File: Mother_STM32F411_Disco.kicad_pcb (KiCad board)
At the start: 2 copper layers, 2 parts

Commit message: boceteando todavia
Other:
- board text added: "Amplificador"
- board text added: "Multiplexor de Audio"
- board text added: "STMF411-Disco"
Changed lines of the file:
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@@
 		)
+	)
+	(gr_rect
+		(start 167 60)
+		(end 215.5 117.5)
+		(stroke
+			(width 0.1)
+			(type default)
+		)
+		(fill no)
+		(layer "F.SilkS")
+	)
+	(gr_rect
+		(start 218 12.75)
+		(end 236 34.25)
+		(stroke
+			(width 0.1)
+			(type default)
+		)
+		(fill no)
+		(layer "F.SilkS")
+	)
+	(gr_rect
+		(start 241 12.75)
+		(end 259 34.25)
+		(stroke
+			(width 0.1)
+			(type default)
+		)
+		(fill no)
+		(layer "F.SilkS")
+	)
+	(gr_rect
+		(start 70.5 24.5)
+		(end 136.5 121.5)
+		(stroke
+			(width 0.1)
+			(type default)
+		)
+		(fill no)
+		(layer "F.SilkS")
+	)
+	(gr_rect
+		(start 194.5 12)
+		(end 212.5 33.5)
+		(stroke
+			(width 0.1)
+			(type default)
+		)
+		(fill no)
+		(layer "F.SilkS")
+	)
+	(gr_text "STMF411-Disco"
+		(at 70.5 121.5 0)
+		(layer "F.SilkS")
+		(effects
+			(font
+				(size 1 1)
+				(thickness 0.1)
+			)
+			(justify left bottom)
+		)
+	)
+	(gr_text "Amplificador"
+		(at 241 34.25 0)
+		(layer "F.SilkS")
+		(effects
+			(font
+				(size 1 1)
+				(thickness 0.1)
+			)
+			(justify left bottom)
+		)
+	)
+	(gr_text "Amplificador"
+		(at 218 34.25 0)
+		(layer "F.SilkS")
+		(effects
+			(font
+				(size 1 1)
+				(thickness 0.1)
+			)
+			(justify left bottom)
+		)
+	)
+	(gr_text "Multiplexor de Audio\n"
+		(at 167 117.5 0)
+		(layer "F.SilkS")
+		(effects
+			(font
+				(size 1 1)
+				(thickness 0.1)
+			)
+			(justify left bottom)
+		)
+	)
+	(gr_text "Amplificador"
+		(at 194.5 33.5 0)
+		(layer "F.SilkS")
+		(effects
+			(font
+				(size 1 1)
+				(thickness 0.1)
+			)
+			(justify left bottom)
+		)
+	)
+	(group ""
+		(members "2fab3fd3-f4d7-4e7b-8b6d-a96610c467cb" "70729842-181e-4080-b271-1663ce8dfaa7")
+	)
+	(group ""
+		(members "d1a54d29-0ff7-45f9-b5e4-6cd1c676e5bf" "e2b95cdf-10a1-4dc4-b970-0cec3a94f96c")
+	)
+	(group ""
+		(members "337aa6e4-fe99-454c-97c6-cfffce0f4d21" "9b0519a3-c9aa-4c5b-8153-00ee1a23a938")
+	)
+	(group ""
+		(members "250b4368-eeb3-4cfe-a6db-56e90e8a5282" "cacae592-f755-4f9d-b2b2-fca2e8c15bf0")
+	)
+	(group ""
+		(members "0da0d133-9946-46c4-b739-db323635e704" "c476d3e7-f70c-42a9-a5f4-4ef6aaca65fd")
 	)
 	(embedded_fonts no)

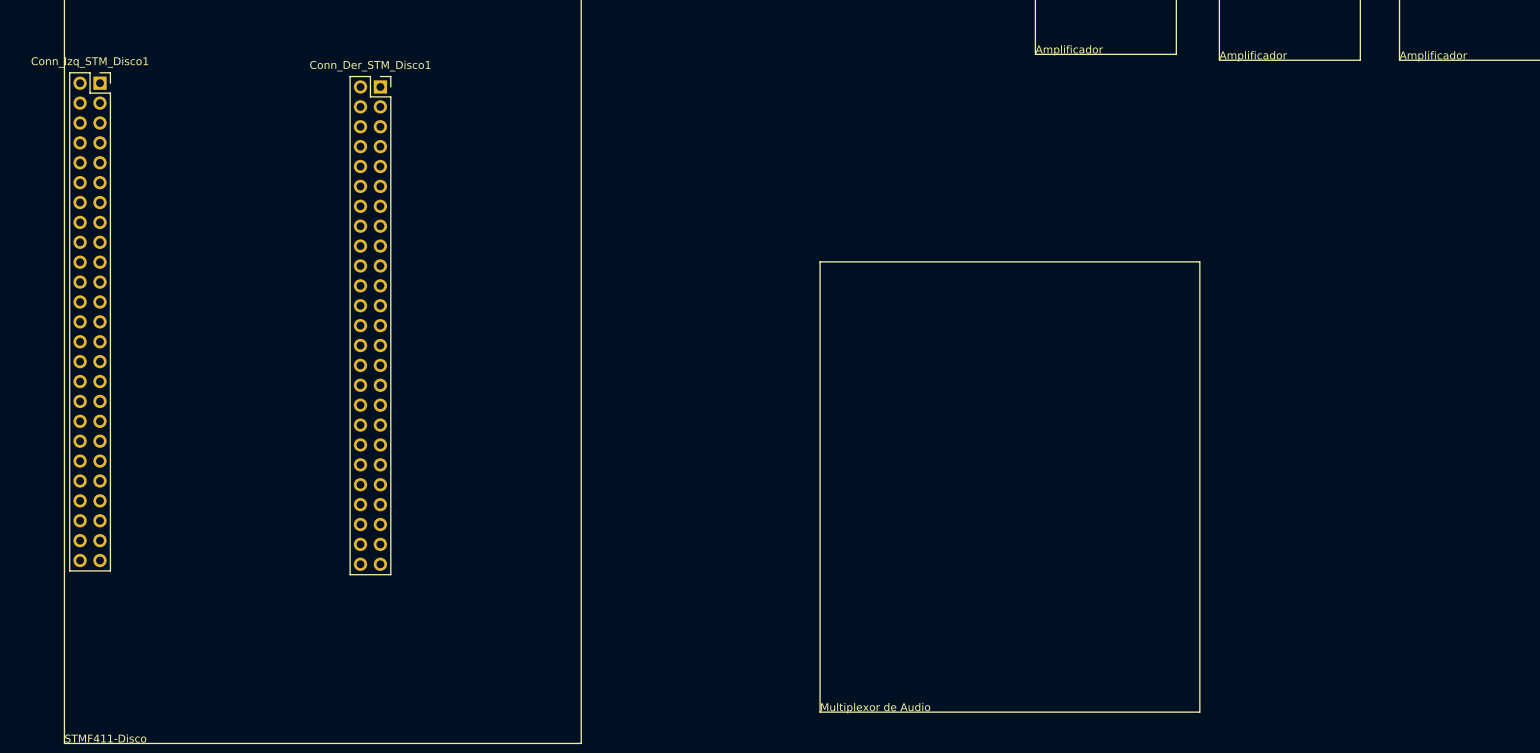
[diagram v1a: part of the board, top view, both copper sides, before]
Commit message: SA-18: placa de esp32 devkitv1 agregada a el esquematico
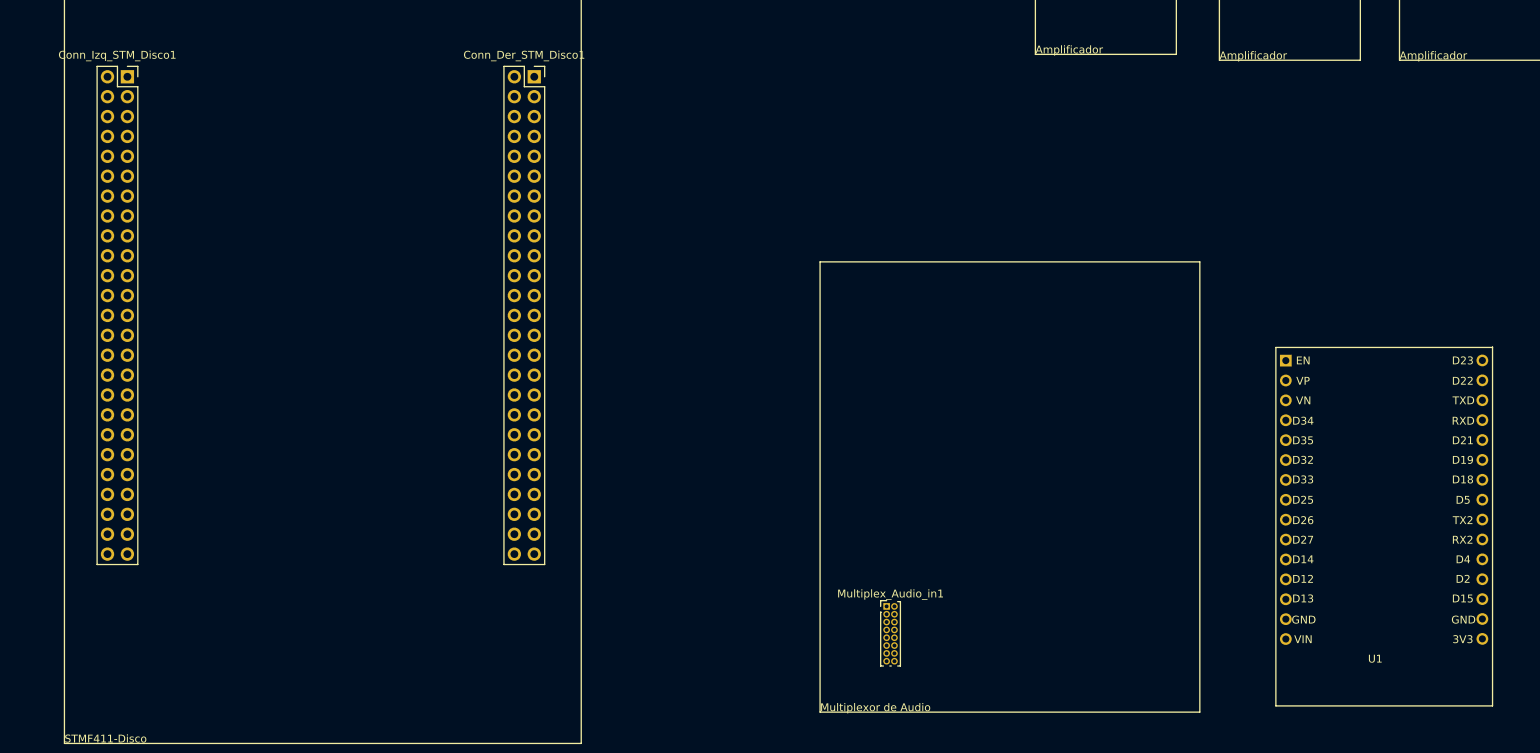
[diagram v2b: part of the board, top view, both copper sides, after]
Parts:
- added Multiplex_Audio_in1: Conn_02x08_Counter_Clockwise, Connector_PinHeader_1.00mm:PinHeader_2x08_P1.00mm_Vertical, F.Cu at (175.5, 104.0)
- added U1: ESP32-DEVKIT-V1, Library:ESP32-C3-DevKitV1, F.Cu at (226.5, 72.6)
- moved Conn_Der_STM_Disco1 19.7 mm to (130.5, 36.4)
- moved Conn_Izq_STM_Disco1 3.59 mm to (78.5, 36.4)

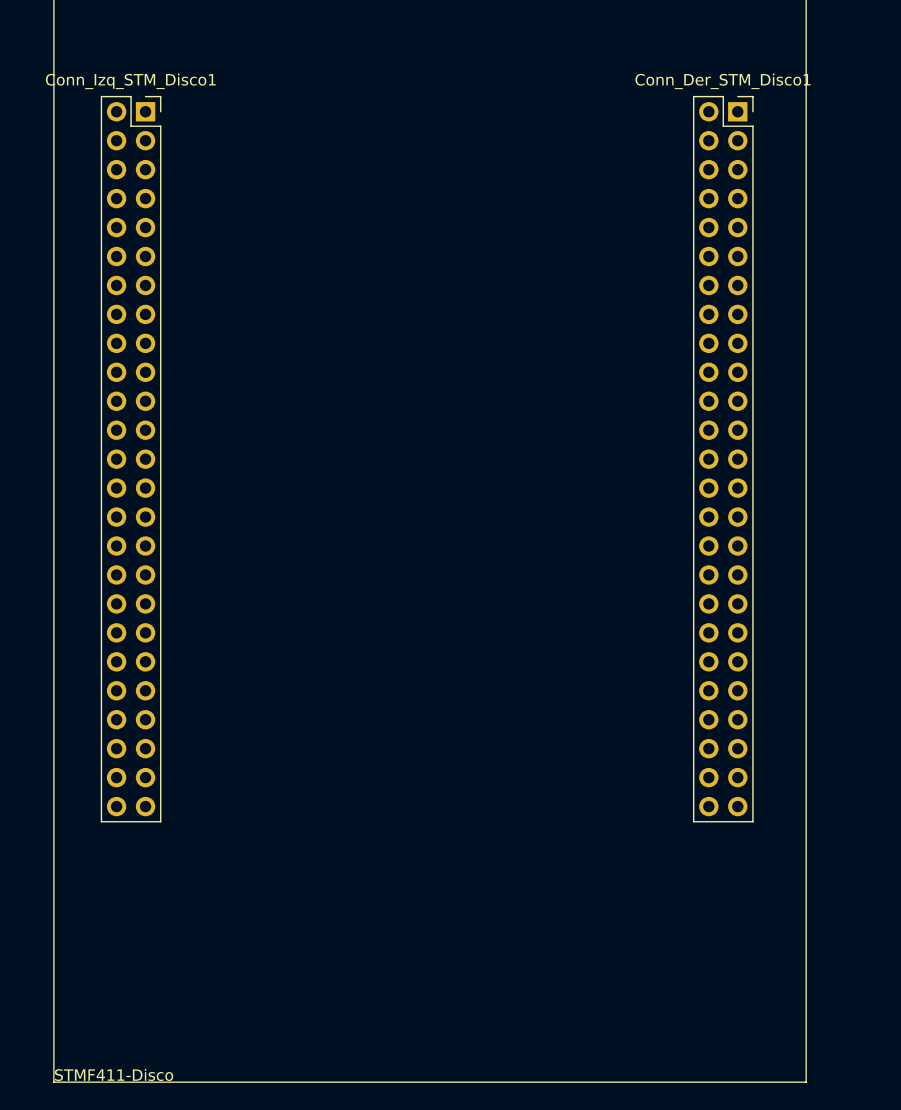
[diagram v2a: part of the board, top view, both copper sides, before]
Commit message: Mudamos librerias a local de proyecto y asignamos 3d models nuevamente
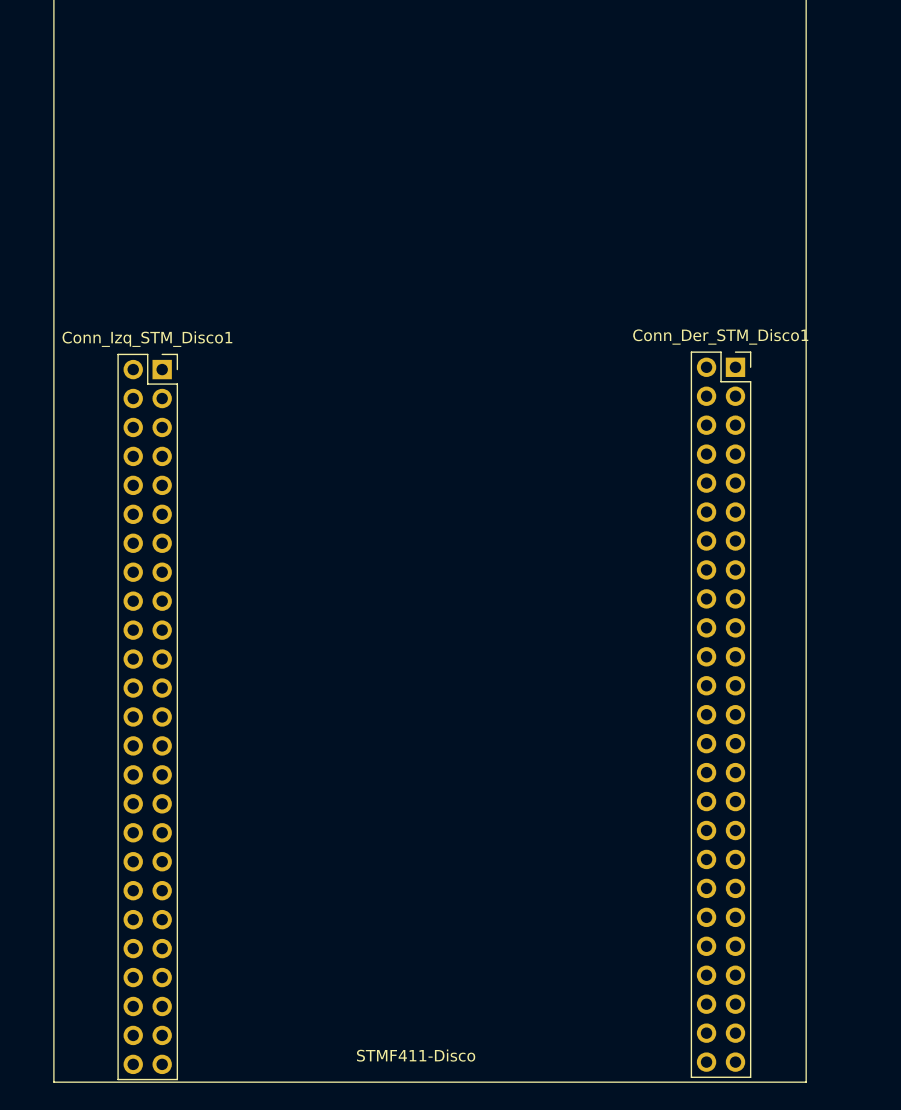
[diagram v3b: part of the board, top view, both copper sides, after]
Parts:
- moved Conn_Izq_STM_Disco1 22.7 mm to (80.0, 59.0)
- moved Conn_Der_STM_Disco1 22.4 mm to (130.3, 58.8)
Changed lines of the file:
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@@
 	(footprint "Connector_PinSocket_2.54mm:PinSocket_2x25_P2.54mm_Vertical"
 		(layer "F.Cu")
-		(at 78.54 36.36)
+		(at 80 58.98)
 		(descr "Through hole straight socket strip, 2x25, 2.54mm pitch, double cols (from Kicad 4.0.7), script generated")
 		(tags "Through hole socket strip THT 2x25 2.54mm double row")
@@
 			)
 		)
+		(model "${KIPRJMOD}/kicad-libraries/3dmodels/stm.3dshapes/STM32F4DISCOVERY--3DModel-STEP-56544.STEP"
+			(offset
+				(xyz 24 -15 8.5)
+			)
+			(scale
+				(xyz 1 1 1)
+			)
+			(rotate
+				(xyz -90 -0 -0)
+			)
+		)
 	)
 	(footprint "Connector_PinSocket_2.54mm:PinSocket_2x25_P2.54mm_Vertical"
 		(layer "F.Cu")
-		(at 130.5 36.36)
+		(at 130.3 58.78)
 		(descr "Through hole straight socket strip, 2x25, 2.54mm pitch, double cols (from Kicad 4.0.7), script generated")
 		(tags "Through hole socket strip THT 2x25 2.54mm double row")
@@
 		)
 		(embedded_fonts no)
-		(model "${KICAD9_3DMODEL_DIR}/RF_Module.3dshapes/ESP32-C3-DevKitM-1.step"
+		(model "${KIPRJMOD}/kicad-libraries/3dmodels/espressif.3dshapes/ESP32-DEVKITC-32D--3DModel-STEP-269445.STEP"
 			(offset
-				(xyz 0 0 0)
+				(xyz 13 -19.5 6)
 			)
 			(scale
@@
 			)
 			(rotate
-				(xyz 0 0 0)
+				(xyz -90 -0 -0)
 			)
 		)
@@
 	)
 	(gr_text "STMF411-Disco"
-		(at 70.5 121.5 0)
+		(at 97 119.8 0)
 		(layer "F.SilkS")
 		(effects
@@
 	)
 	(group ""
-		(members "250b4368-eeb3-4cfe-a6db-56e90e8a5282" "cacae592-f755-4f9d-b2b2-fca2e8c15bf0")
+		(members "0da0d133-9946-46c4-b739-db323635e704" "c476d3e7-f70c-42a9-a5f4-4ef6aaca65fd")
 	)
 	(group ""
-		(members "0da0d133-9946-46c4-b739-db323635e704" "c476d3e7-f70c-42a9-a5f4-4ef6aaca65fd")
+		(members "250b4368-eeb3-4cfe-a6db-56e90e8a5282" "cacae592-f755-4f9d-b2b2-fca2e8c15bf0")
 	)
 	(embedded_fonts no)

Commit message: .sch mergeado
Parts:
- added 1_Out_Ampl1: Conn_01x02, Connector_PinSocket_2.54mm:PinSocket_1x02_P2.54mm_Vertical, F.Cu at (91.6, 137.3)
- added 1_Out_Ampl2: Conn_01x02, Connector_PinSocket_2.54mm:PinSocket_1x02_P2.54mm_Vertical, F.Cu at (96.2, 137.3)
- added 1_Out_Ampl3: Conn_01x02, Connector_PinSocket_2.54mm:PinSocket_1x02_P2.54mm_Vertical, F.Cu at (100.8, 137.3)
- added 2_Out_Ampl1: Conn_01x02, Connector_PinSocket_2.54mm:PinSocket_1x02_P2.54mm_Vertical, F.Cu at (105.4, 137.3)
- added 2_Out_Ampl2: Conn_01x02, Connector_PinSocket_2.54mm:PinSocket_1x02_P2.54mm_Vertical, F.Cu at (110.0, 137.3)
- added 2_Out_Ampl3: Conn_01x02, Connector_PinSocket_2.54mm:PinSocket_1x02_P2.54mm_Vertical, F.Cu at (114.6, 137.3)
- added Audio_IN_Ampl1: Conn_01x03, Connector_PinSocket_2.54mm:PinSocket_1x03_P2.54mm_Vertical, F.Cu at (91.6, 144.4)
- added Audio_IN_Ampl2: Conn_01x03, Connector_PinSocket_2.54mm:PinSocket_1x03_P2.54mm_Vertical, F.Cu at (96.2, 144.4)
- added Audio_IN_Ampl3: Conn_01x03, Connector_PinSocket_2.54mm:PinSocket_1x03_P2.54mm_Vertical, F.Cu at (100.8, 144.4)
- added Multiplex_Audio_out_1: Conn_01x03, Connector_PinSocket_2.54mm:PinSocket_1x03_P2.54mm_Vertical, F.Cu at (105.4, 144.4)
- added Multiplex_Audio_out_2: Conn_01x03, Connector_PinSocket_2.54mm:PinSocket_1x03_P2.54mm_Vertical, F.Cu at (110.0, 144.4)
- added Multiplex_Audio_out_3: Conn_01x03, Connector_PinSocket_2.54mm:PinSocket_1x03_P2.54mm_Vertical, F.Cu at (114.6, 144.4)
- added Out_Speaker_1: Conn_01x02, Connector_PinHeader_2.54mm:PinHeader_1x02_P2.54mm_Horizontal, F.Cu at (78.2, 137.2)
- added Out_Speaker_2: Conn_01x02, Connector_PinHeader_2.54mm:PinHeader_1x02_P2.54mm_Horizontal, F.Cu at (78.2, 144.4)
- added Out_Speaker_3: Conn_01x02, Connector_PinHeader_2.54mm:PinHeader_1x02_P2.54mm_Horizontal, F.Cu at (78.2, 151.5)
- added Out_Speaker_4: Conn_01x02, Connector_PinHeader_2.54mm:PinHeader_1x02_P2.54mm_Horizontal, F.Cu at (78.2, 158.7)
- added Out_Speaker_5: Conn_01x02, Connector_PinHeader_2.54mm:PinHeader_1x02_P2.54mm_Horizontal, F.Cu at (78.2, 165.8)
- added Out_Speaker_6: Conn_01x02, Connector_PinHeader_2.54mm:PinHeader_1x02_P2.54mm_Horizontal, F.Cu at (78.2, 172.9)
- added PWR_Ampl1: Conn_01x02, Connector_PinSocket_2.54mm:PinSocket_1x02_P2.54mm_Vertical, F.Cu at (119.2, 137.3)
- added PWR_Ampl2: Conn_01x02, Connector_PinSocket_2.54mm:PinSocket_1x02_P2.54mm_Vertical, F.Cu at (123.8, 137.3)
- added PWR_Ampl3: Conn_01x02, Connector_PinSocket_2.54mm:PinSocket_1x02_P2.54mm_Vertical, F.Cu at (128.4, 137.3)
- added Pantalla-Botones1: Conn_01x08, Connector_PinSocket_2.54mm:PinSocket_1x08_P2.54mm_Vertical, F.Cu at (91.6, 154.1)

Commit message: Merge pcb listo
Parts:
- moved Pantalla-Botones1 132.2 mm to (220.3, 124.0)
- moved Audio_IN_Ampl1 102.4 mm to (60.5, 46.8)
- moved PWR_Ampl1 97.5 mm to (60.5, 59.5)
- moved 1_Out_Ampl1 91.3 mm to (79.0, 46.8)
- moved Out_Speaker_6 83.8 mm to (24.2, 108.8)
- moved Out_Speaker_2 83.8 mm to (24.2, 80.3)
- moved Out_Speaker_4 83.8 mm to (24.2, 94.5)
- moved Out_Speaker_1 83.8 mm to (24.2, 73.1)
- moved Out_Speaker_3 83.8 mm to (24.2, 87.4)
- moved Out_Speaker_5 83.8 mm to (24.2, 101.7)
- moved 2_Out_Ampl1 82.2 mm to (78.9, 59.5)
- moved PWR_Ampl2 76.2 mm to (57.0, 100.5)
- moved PWR_Ampl3 72.9 mm to (56.7, 123.9)
- moved Conn_Der_STM_Disco1 69.5 mm to (197.4, 76.9)
- moved Conn_Izq_STM_Disco1 69.5 mm to (147.1, 77.1)
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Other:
- board text added: "AMPL_1 PAM8403"
- board text added: "AMPL_2 PAM8403"
- board text added: "AMPL_3 PAM8403"
- board text removed: "Amplificador"

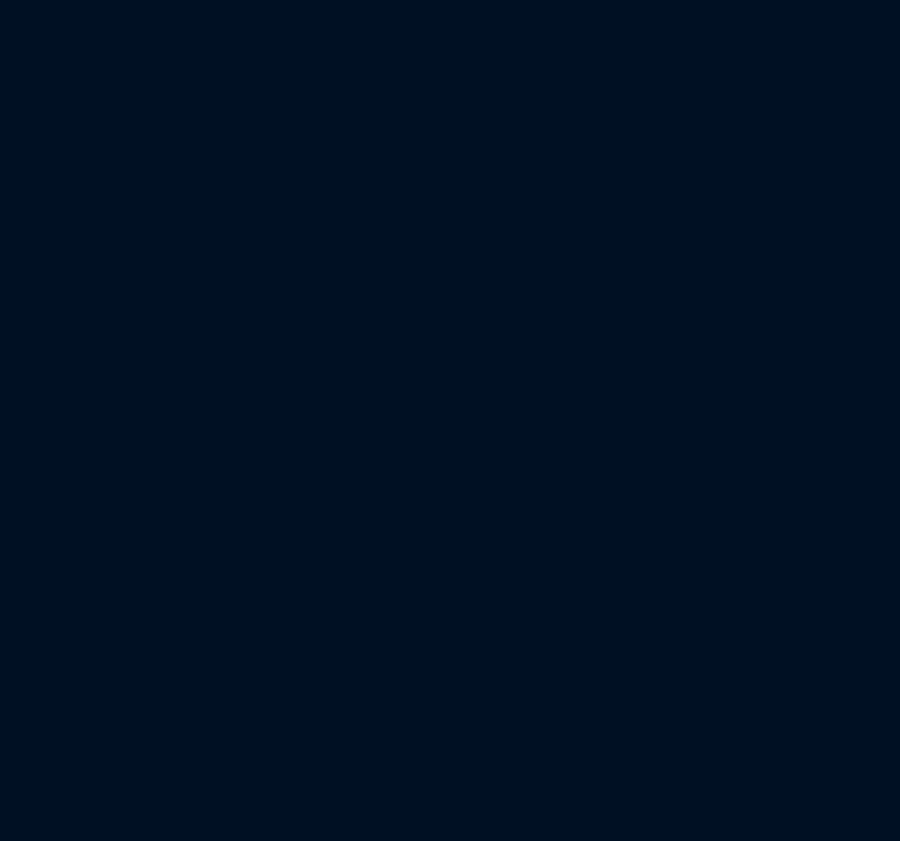
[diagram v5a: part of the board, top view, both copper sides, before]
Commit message: UART STM conectada
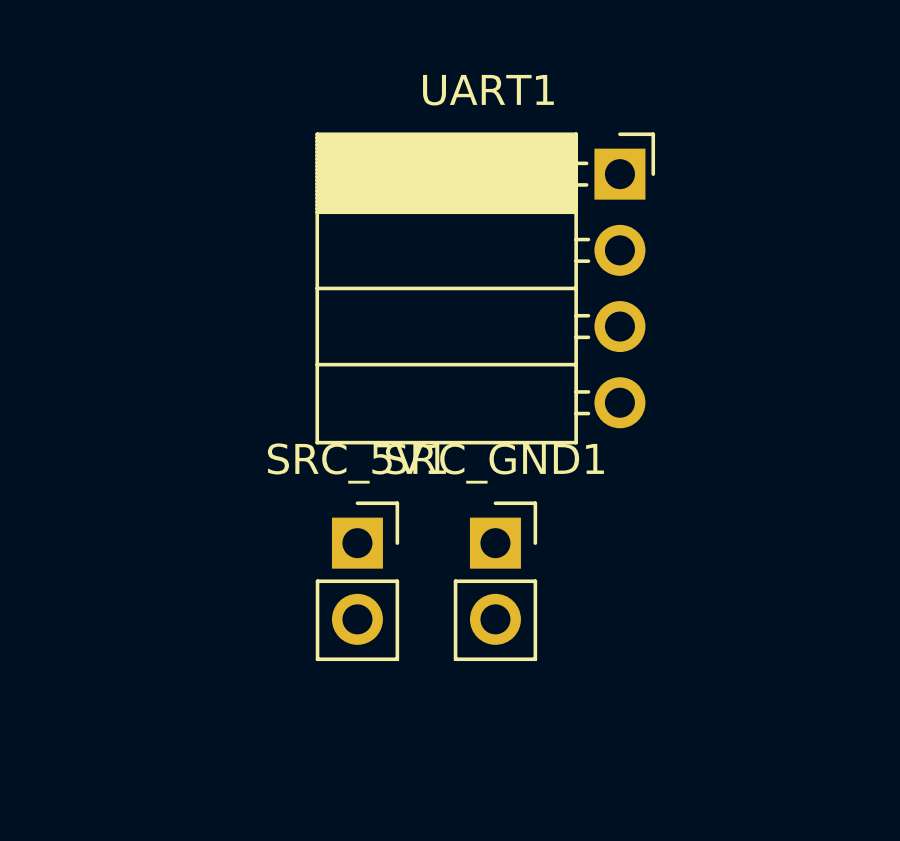
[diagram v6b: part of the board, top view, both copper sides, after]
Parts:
- added SRC_5V1: Conn_01x02, Connector_PinSocket_2.54mm:PinSocket_1x02_P2.54mm_Vertical, F.Cu at (106.3, 53.7)
- added SRC_GND1: Conn_01x02, Connector_PinSocket_2.54mm:PinSocket_1x02_P2.54mm_Vertical, F.Cu at (110.9, 53.7)
- added UART1: Conn_01x04, Connector_PinSocket_2.54mm:PinSocket_1x04_P2.54mm_Horizontal, F.Cu at (115.0, 41.4)
